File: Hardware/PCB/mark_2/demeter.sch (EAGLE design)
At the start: 28 parts, among them IC1 4050, IC2 LM1117-5.0, IC3 LM1117-3.3, IC4 M24C64, IC5 MCP3424, IC6 MCP23017SO, Q1 IRLML6402, Q2 IRLML6402

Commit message: 
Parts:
- removed R3: (no value), mark_2:R-EU_R0805
- added D4, D5, D6, D7, D8, D9: MBR0520, mark_2:MBR0520
- added IC7: MAX485, mark_2:MAX485
- added JK2, JK3, JK4: (no value), mark_2:AUDIO-JACK2PTH
- added Q3, Q4, Q5, Q6, Q7, Q8: IRLML6402, mark_2:IRLML6402
- added R5, R6, R7: (no value), mark_2:R-EU_R0805
- U$2: value MAX485 -> ATMEGA32U4-AU; device mark_2:MAX485 -> mark_2:ATMEGA32U4-AU
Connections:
- new net N$15: JK2.TIP, Q3.D, Q4.D
- new net N$16: D4.C, Q3.S
- new net N$17: D5.C, Q4.S
- new net N$18: JK3.TIP, Q5.D, Q6.D
- new net N$19: D6.C, Q5.S
- new net N$20: D7.C, Q6.S
- new net N$21: JK4.TIP, Q7.D, Q8.D
- new net N$22: D8.C, Q7.S
- new net N$23: D9.C, Q8.S
- net +3V3: now also D5.A, D7.A, D9.A
- net +5V: now also D4.A, D6.A, D8.A, IC7.VCC, U$2.AVCC, U$2.AVCC1, U$2.UVCC, U$2.VCC1
- net CH2: now also JK2.RING
- net CH3: now also JK3.RING
- net CH4: now also JK4.RING
- net EN: now also IC7.DE, IC7.RE; no longer U$2.DE, U$2.RE
- net EN2-3: now also Q4.G
- net EN2-5: now also Q3.G
- net EN3-3: now also Q6.G
- net EN3-5: now also Q5.G
- net EN4-3: now also Q8.G
- net EN4-5: now also Q7.G
- net GND: now also IC7.GND, JK2.SLEEVE, JK3.SLEEVE, JK4.SLEEVE, R5.1, R6.1, R7.1, U$2.GND1, U$2.GND2, U$2.GND3, U$2.UGND
- net N$2: now also IC7.B; no longer R3.2, U$2.B
- net N$5: now also IC7.A; no longer R3.1, U$2.A
- net RXD: now also IC7.DI; no longer U$2.DI
- net SN2: now also JK2.TSH, R5.2
- net SN3: now also JK3.TSH, R6.2
- net SN4: now also JK4.TSH, R7.2
- net TXD: now also IC7.RO; no longer U$2.RO
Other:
- note added: "DAC"
- moved on the sheet: C2, C3, C4, C5, C6, C7, D1, D2, D3, IC1A, IC1B, IC1C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

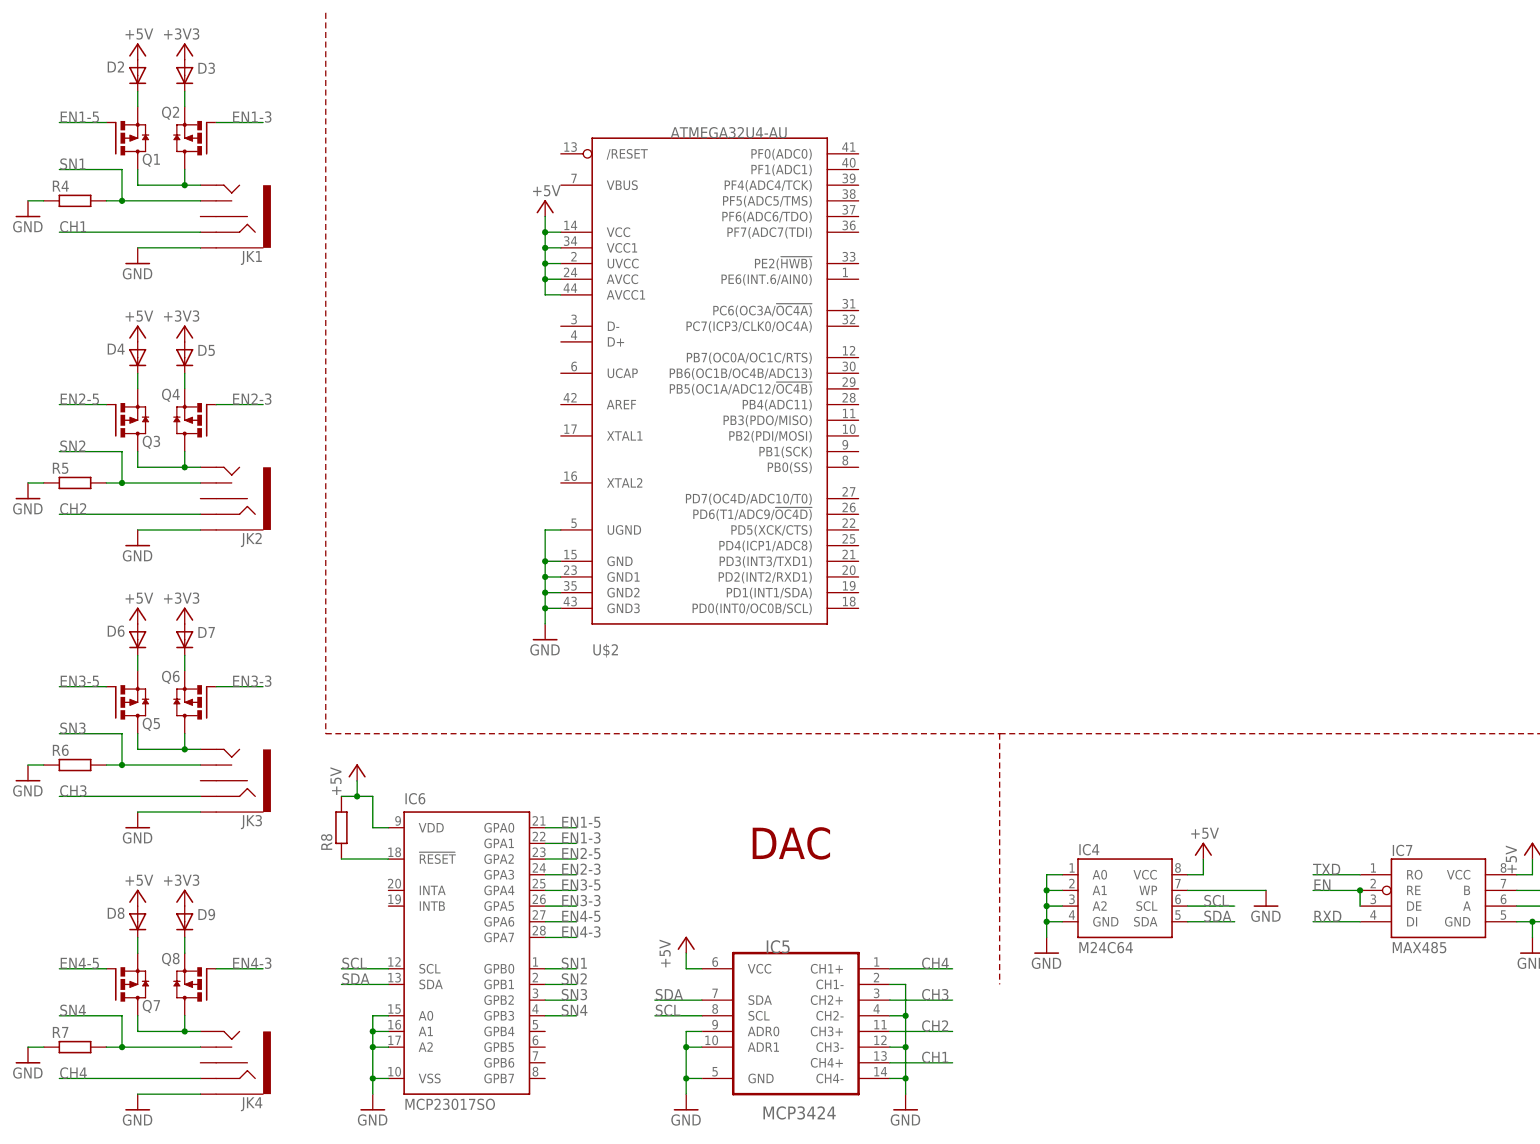
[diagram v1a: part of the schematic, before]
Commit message: 
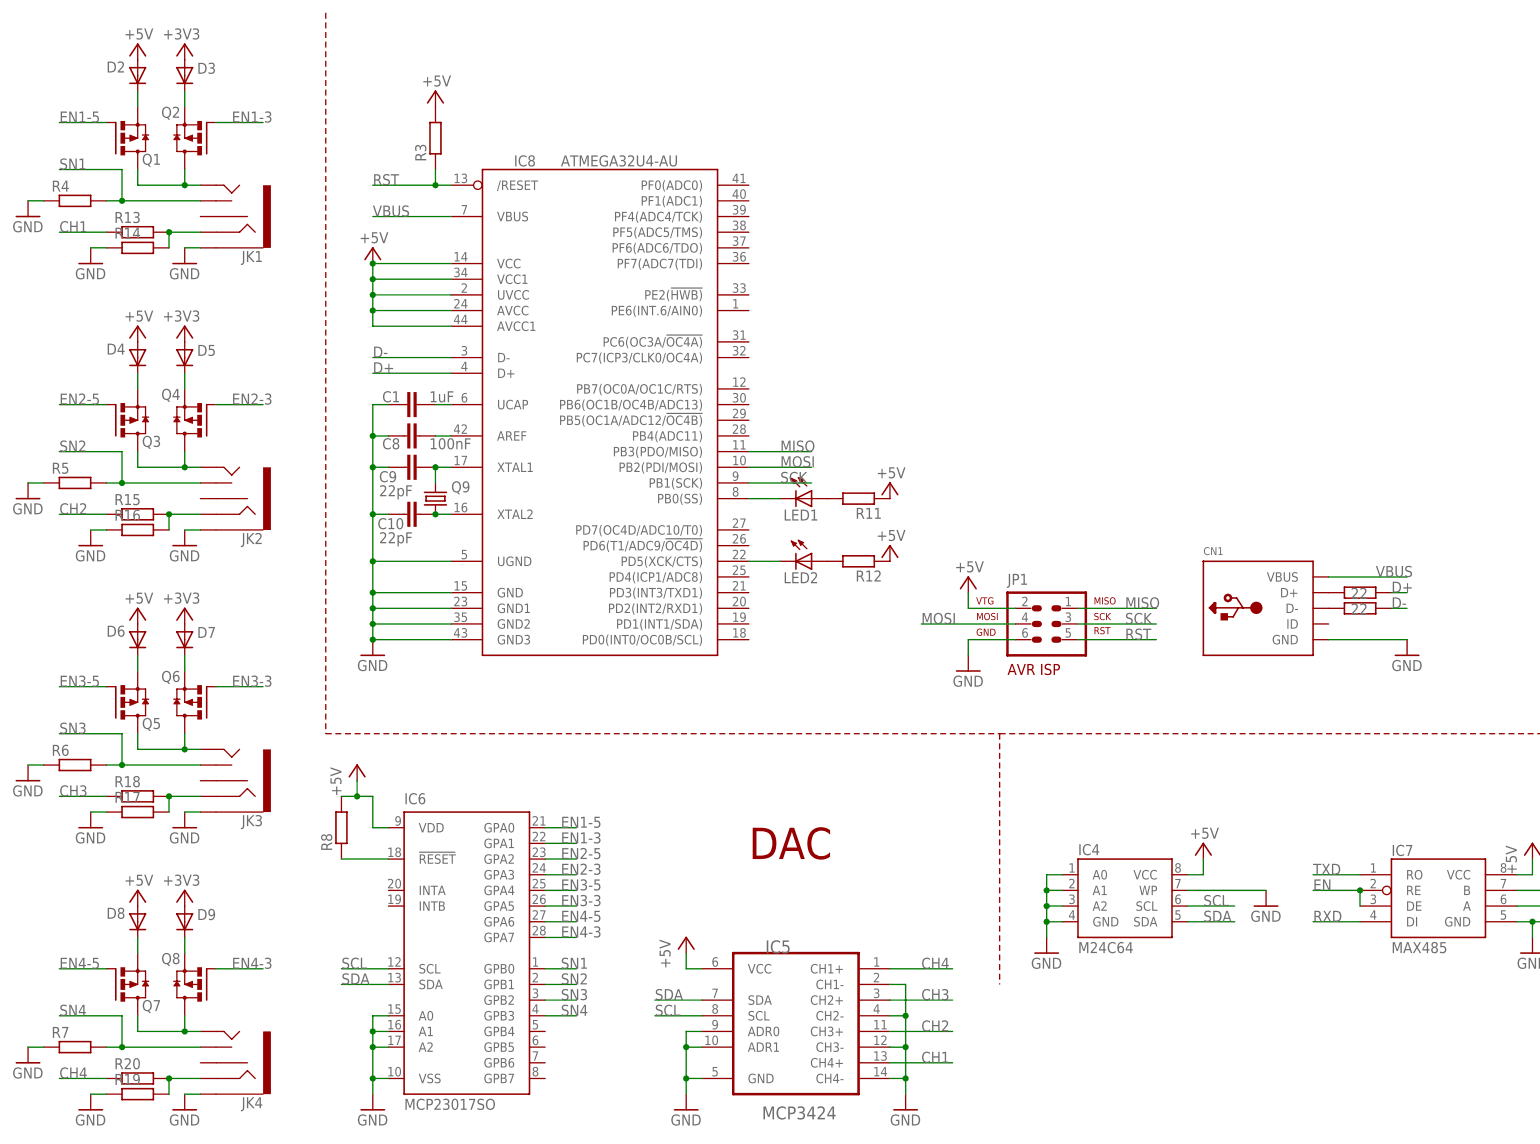
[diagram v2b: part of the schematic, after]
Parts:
- removed U$2: ATMEGA32U4-AU, mark_2:ATMEGA32U4-AU
- added C1: 1uF, mark_2:C-EUC0805K
- added C10, C9: 22pF, mark_2:C-EUC0805K
- added C8: 100nF, mark_2:C-EUC0805K
- added CN1: (no value), mark_2:USBMINIB
- added IC8: ATMEGA32U4-AU, mark_2:ATMEGA32U4-AU
- added JP1: AVR-ISP-6, mark_2:AVR-ISP-6
- added LED1, LED2: (no value), mark_2:LED0805
- added Q9: (no value), mark_2:CRYSTALHC49UP
- added R10, R9: 22, mark_2:R-EU_R0805
- added R11, R12, R13, R14, R15, R16, R17, R18, R19, R20, R3: (no value), mark_2:R-EU_R0805
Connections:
- new net D+: IC8.D+, R9.1
- new net D-: IC8.D-, R10.1
- new net MISO: IC8.PB3(PDO/MISO), JP1.MISO
- new net MOSI: IC8.PB2(PDI/MOSI), JP1.MOSI
- new net N$24: C1.1, IC8.UCAP
- new net N$25: C8.1, IC8.AREF
- new net N$26: C9.1, IC8.XTAL1, Q9.2
- new net N$27: C10.1, IC8.XTAL2, Q9.1
- new net N$28: CN1.D+, R9.2
- new net N$29: CN1.D-, R10.2
- new net N$30: JK1.RING, R13.2, R14.2
- new net N$31: LED1.A, R11.2
- new net N$32: JK2.RING, R15.2, R16.2
- new net N$33: LED2.A, R12.2
- new net N$34: JK3.RING, R17.2, R18.2
- new net N$35: JK4.RING, R19.2, R20.2
- new net RST: IC8./RESET, JP1.RST, R3.1
- new net RXLED: IC8.PB0(SS), LED1.C
- new net SCK: IC8.PB1(SCK), JP1.SCK
- new net TXLED: IC8.PD5(XCK/CTS), LED2.C
- new net VBUS: CN1.VBUS, IC8.VBUS
- net +5V: now also IC8.AVCC, IC8.AVCC1, IC8.UVCC, IC8.VCC, IC8.VCC1, JP1.VTG, R11.1, R12.1, R3.2; no longer U$2.AVCC, U$2.AVCC1, U$2.UVCC, U$2.VCC, U$2.VCC1
- net CH1: now also R13.1; no longer JK1.RING
- net CH2: now also R15.1; no longer JK2.RING
- net CH3: now also R18.1; no longer JK3.RING
- net CH4: now also R20.1; no longer JK4.RING
- net GND: now also C1.2, C10.2, C8.2, C9.2, CN1.GND, IC8.GND, IC8.GND1, IC8.GND2, IC8.GND3, IC8.UGND, JP1.GND, R14.1, R16.1, R17.1, R19.1; no longer U$2.GND, U$2.GND1, U$2.GND2, U$2.GND3, U$2.UGND

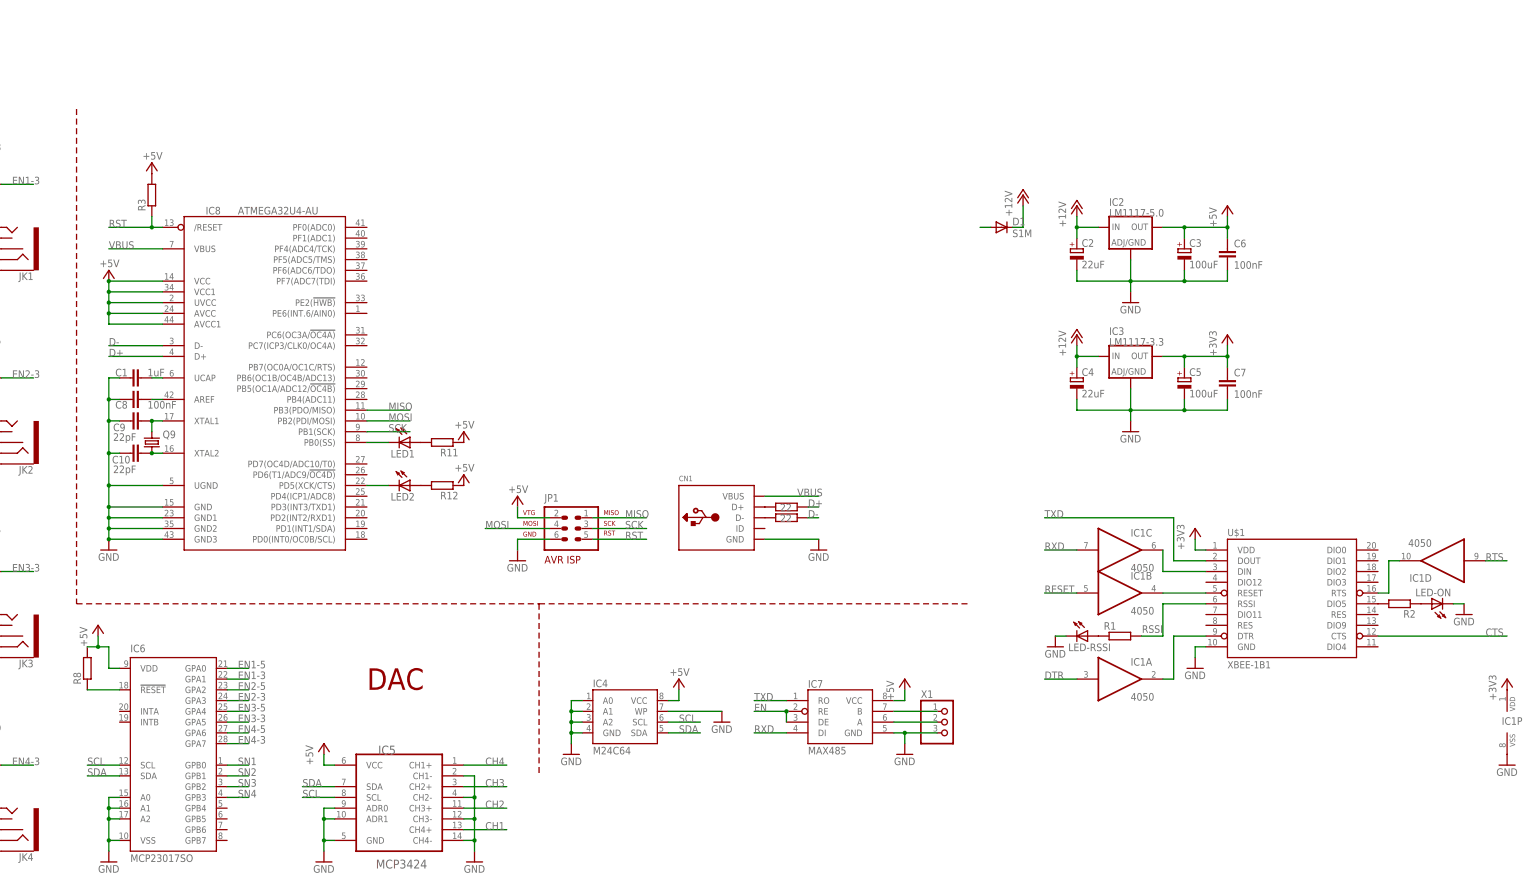
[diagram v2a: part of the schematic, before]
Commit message: 
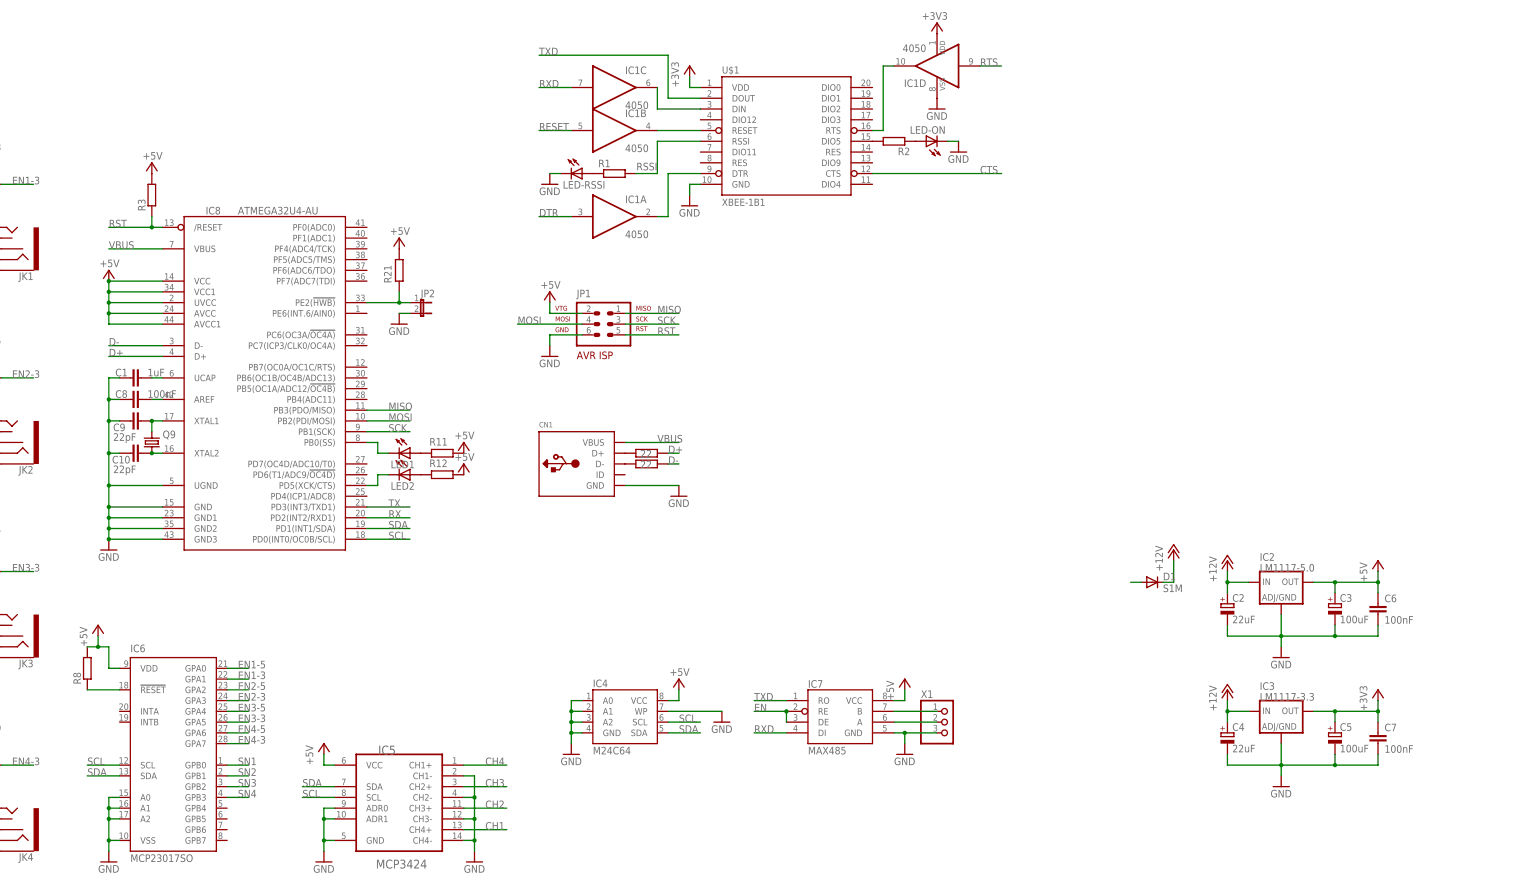
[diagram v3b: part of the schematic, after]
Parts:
- added JP2: (no value), mark_2:JUMPER-2SMD-NO
- added R21: (no value), mark_2:R-EU_R0805
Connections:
- new net N$36: IC8.PE2(!HWB), JP2.1, R21.2
- new net RX: IC8.PD2(INT2/RXD1)
- new net TX: IC8.PD3(INT3/TXD1)
- net +5V: now also R21.1
- net GND: now also JP2.2
- net SCL: now also IC8.PD0(INT0/OC0B/SCL)
- net SDA: now also IC8.PD1(INT1/SDA)
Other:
- note removed: "DAC"
- moved on the sheet: C2, C3, C4, C5, C6, C7, CN1, D1, IC1A, IC1B, IC1C, IC1D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
